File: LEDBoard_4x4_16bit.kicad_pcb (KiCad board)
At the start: 2 copper layers, 40 x 40 mm, 34 parts, among them J1 VCC_in, J2 GND_in, J3 signal_in, J4 VCC_out, J5 GND_out, J6 signal_out, U1 TLC5971RGER, U2 TLC5971RGER, U3 TLC5971RGER, U4 TLC5971RGER

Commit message: pcb parts all positioned
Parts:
- removed the J1 at (52.0, 60.0)
- removed J4: VCC_out, Socket_Strips:Socket_Strip_Angled_1x01_Pitch2.54mm
- removed J5: GND_out, Socket_Strips:Socket_Strip_Angled_1x01_Pitch2.54mm
- added C5: 47uF, Capacitors_SMD:C_0603, F.Cu at (70.0, 67.5)
- added HS1: Heatsink, Oddities:Dummy_Empty, F.Cu at (92.0, 90.0)
- added MK1: Mounting_Hole, Mounting_Holes:MountingHole_2.7mm_M2.5_Pad_Via, F.Cu at (60.0, 68.0)
- added MK2: Mounting_Hole, Mounting_Holes:MountingHole_2.7mm_M2.5_Pad_Via, F.Cu at (80.0, 68.0)
- J1: renamed from J3; moved to B.Cu
- J2: value GND_in -> power; footprint Socket_Strips:Socket_Strip_Angled_1x01_Pitch2.54mm -> Socket_Strips:Socket_Strip_Straight_1x06_Pitch2.54mm; moved to B.Cu
- J6: footprint Socket_Strips:Socket_Strip_Angled_1x02_Pitch2.54mm -> Socket_Strips:Socket_Strip_Straight_1x02_Pitch2.54mm; moved to B.Cu
- R1: value R -> 2k7 1%
- U1, U2, U3, U4: footprint Housings_DFN_QFN:QFN-24-1EP_4x4mm_Pitch0.5mm -> Housings_DFN_QFN:Texas_S-PVQFN-N24_ThermalVias
- moved J6 17.1 mm to (83.7, 88.0), turned to 270 degrees
- moved J1 16.8 mm to (53.7, 88.0), turned to 270 degrees
- moved J2 14.1 mm to (63.6, 88.0), turned to 270 degrees
- moved C4 10.2 mm to (85.0, 79.0), turned to 0 degrees
- moved R4 10.2 mm to (85.0, 77.0), turned to 0 degrees
- moved R1 4.12 mm to (65.0, 57.0)
- moved C3 2.24 mm to (65.0, 79.0)
- moved R2 2.24 mm to (85.0, 57.0)
- moved R3 2.24 mm to (65.0, 77.0)
- moved C2 2.14 mm to (85.0, 59.0)
- moved D1.1 2.00 mm to (55.0, 53.0)
- moved D1.2 2.00 mm to (55.0, 63.0)
- moved D1.3 2.00 mm to (55.0, 73.0)
- moved D1.4 2.00 mm to (55.0, 83.0)
- moved D2.1 2.00 mm to (65.0, 53.0)
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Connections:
- J2 pad 1: GND -> VCC
- U2 pad 6: /data_1-2 -> Net-(U2-Pad6)
- U3 pad 6: /data_2-3 -> Net-(U3-Pad6)
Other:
- board text added: "17.04.2017"
- board text added: "17.07. 2017"
- board text added: "LEDBoard 4x4 16bit"
- board text added: "LEDBoard_4x4_16bit cc by s-light.eu"
- board text added: "cc by s-light.eu"

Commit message: pcb started routing
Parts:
- D1.1, D1.2, D1.3, D1.4, D2.1, D2.2, D2.3, D2.4, D3.1, D3.2, D3.3, D3.4, D4.1, D4.2, D4.3, D4.4: footprint nichia:LED_NSSM032AT_wViaHeatSink -> nichia:LED_NSSM032AT_wViaHeatSinkBig
- MK1, MK2: footprint Mounting_Holes:MountingHole_2.7mm_M2.5_Pad_Via -> Mounting_Holes:MountingHole_3.2mm_M3_ISO7380_Pad
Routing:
- net VCC: track 0.00 -> 184.3 mm
- net GND: track 0.00 -> 88.3 mm
- net /LED_3.1_G: track 0.00 -> 35.7 mm, vias 0 -> 4
- net /LED_4.1_B: track 0.00 -> 35.0 mm
- net /LED_3.2_R: track 0.00 -> 33.8 mm, vias 0 -> 4
- net /LED_3.1_B: track 0.00 -> 33.6 mm, vias 0 -> 4
- net /LED_4.1_G: track 0.00 -> 32.1 mm
- net /LED_4.1_R: track 0.00 -> 31.0 mm
- net /LED_3.1_R: track 0.00 -> 30.8 mm, vias 0 -> 4
- net /LED_3.2_G: track 0.00 -> 30.1 mm, vias 0 -> 4
- net /LED_4.2_R: track 0.00 -> 28.1 mm
- net /LED_3.2_B: track 0.00 -> 26.6 mm, vias 0 -> 4
- net /LED_4.2_G: track 0.00 -> 22.4 mm
- net /LED_4.2_B: track 0.00 -> 16.8 mm
- net Net-(U2-Pad6): track 0.00 -> 10.7 mm, vias 0 -> 4
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
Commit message: pcb routing almost finished
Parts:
- moved C5 0.50 mm to (70.0, 68.0)
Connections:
- U4 pad 6: Net-(U4-Pad6) -> /data_out
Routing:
- net VCC: track 184.3 -> 325.1 mm
- net GND: track 88.3 -> 199.4 mm, vias 0 -> 6
- net /clock_in: track 0.00 -> 41.4 mm, vias 0 -> 1
- net /data_in: track 0.00 -> 40.4 mm, vias 0 -> 1
- net /data_1-2: track 0.00 -> 36.7 mm, vias 0 -> 3
- net /clock_1-2: track 10.7 -> 42.7 mm
- net /LED_3.1_G: track 35.7 -> 8.92 mm, vias 4 -> 1
- net /LED_4.1_B: track 35.0 -> 8.74 mm
- net /LED_3.2_R: track 33.8 -> 8.45 mm, vias 4 -> 1
- net /LED_3.1_B: track 33.6 -> 8.39 mm, vias 4 -> 1
- net /clock_2-3: track 0.00 -> 24.6 mm, vias 0 -> 4
- net /data_2-3: track 0.00 -> 24.5 mm, vias 0 -> 3
- net /LED_4.1_G: track 32.1 -> 8.02 mm
- net /LED_4.1_R: track 31.0 -> 7.76 mm
- net /LED_3.1_R: track 30.8 -> 7.69 mm, vias 4 -> 1
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- added copper zone on F.Cu, net GND
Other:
- net class signal added: clearance 0.15, trace_width 0.2, via_dia 0.6, via_drill 0.3

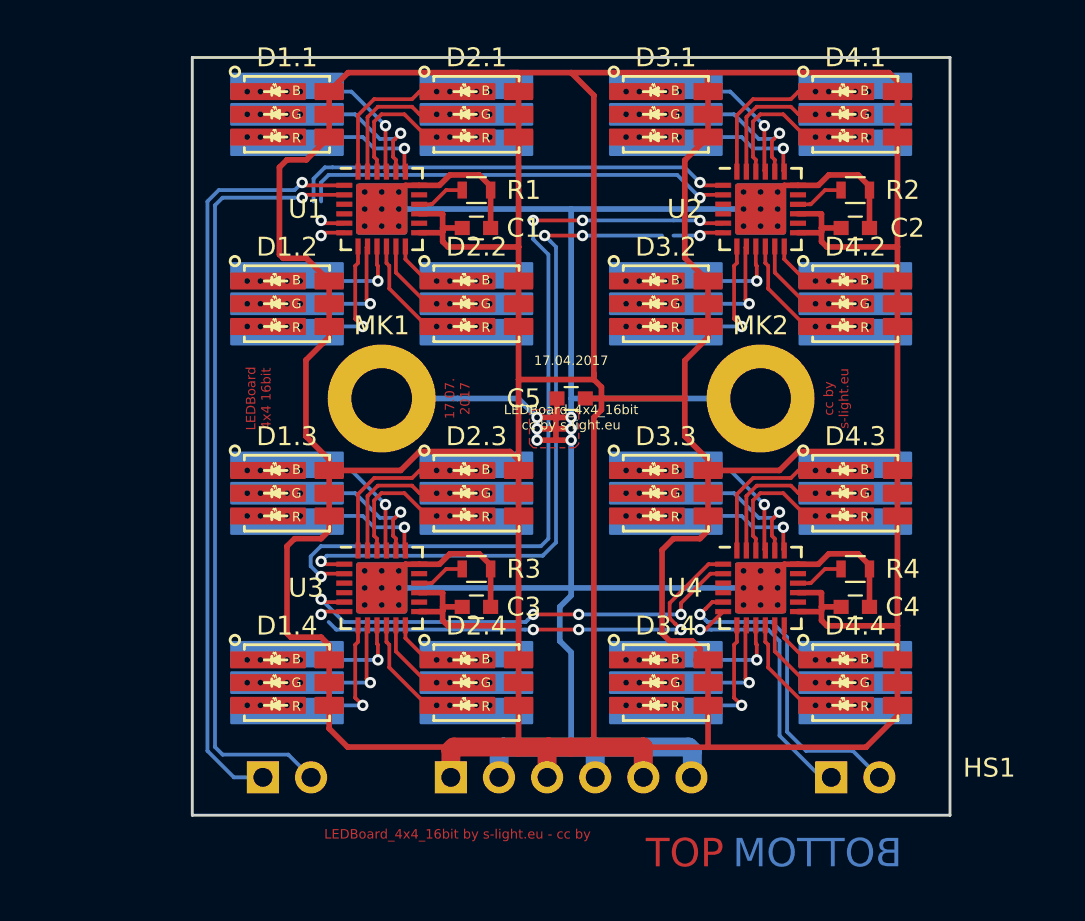
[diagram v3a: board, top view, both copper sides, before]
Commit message: pcb tried to fix missing net links
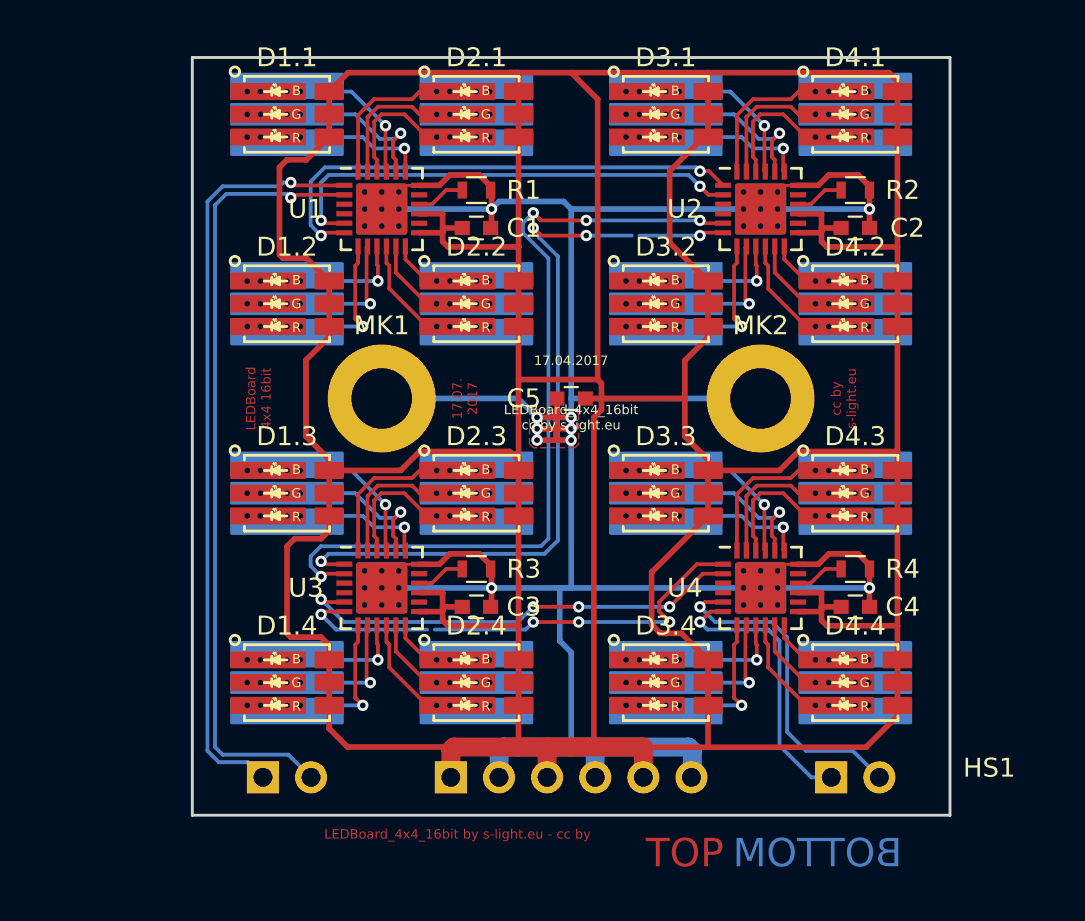
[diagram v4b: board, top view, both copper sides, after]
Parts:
- R2, R3, R4: value R -> 2k7 1%
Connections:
- net /data_1-2 renamed /data_intern_2
- net Net-(R1-Pad1) renamed /U1_sense
- net Net-(R2-Pad1) renamed /U2_sense
- net Net-(R3-Pad1) renamed /U3_sense
- net Net-(R4-Pad1) renamed /U4_sense
- U4 pad 1: /data_2-3 -> Net-(U3-Pad6)
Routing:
- net GND: track 199.4 -> 160.4 mm, vias 6 -> 10
- net /data_2-3: track 24.5 -> 0.00 mm, vias 3 -> 0
- net Net-(U3-Pad6): track 1.29 -> 25.3 mm, vias 1 -> 4
- net /LED_4.4_B: track 4.20 -> 7.30 mm
- net /LED_4.4_R: track 7.02 -> 10.1 mm
- net /LED_4.4_G: track 5.61 -> 8.41 mm
- net /data_0-1: track 24.8 -> 26.8 mm
- net Net-(U2-Pad6): track 2.69 -> 4.49 mm
- net /clock_1-2: track 42.7 -> 43.8 mm
- net /clock_0-1: track 24.2 -> 25.2 mm
- net /clock_2-3: track 24.6 -> 24.1 mm
- added copper zone on B.Cu, net GND
- added copper zone on F.Cu, net VCC

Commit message: pcb fixed broken net data_2-3
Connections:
- net /data_intern_2 renamed /data_1-2
- net Net-(U3-Pad6) renamed /data_2-3

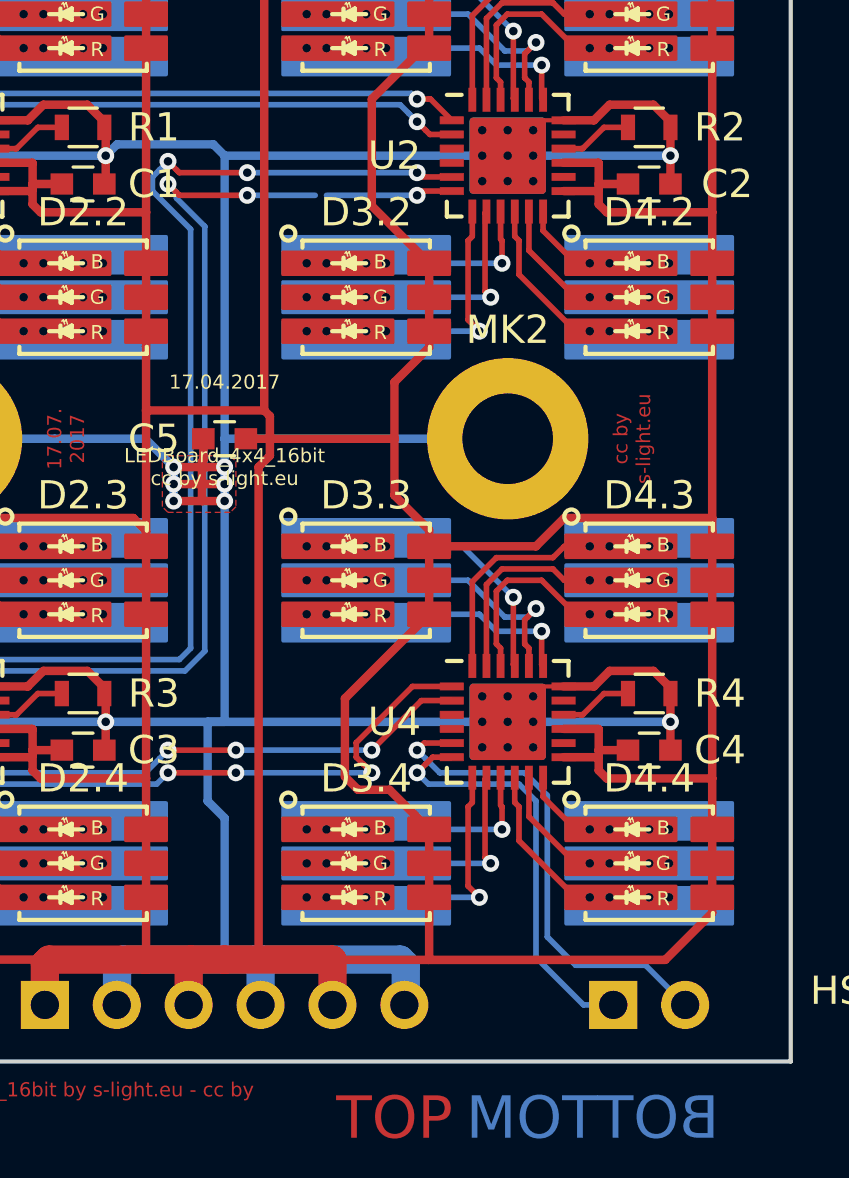
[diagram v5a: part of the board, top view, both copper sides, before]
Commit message: fixed net data_1-2 (manually hand edited net-file)
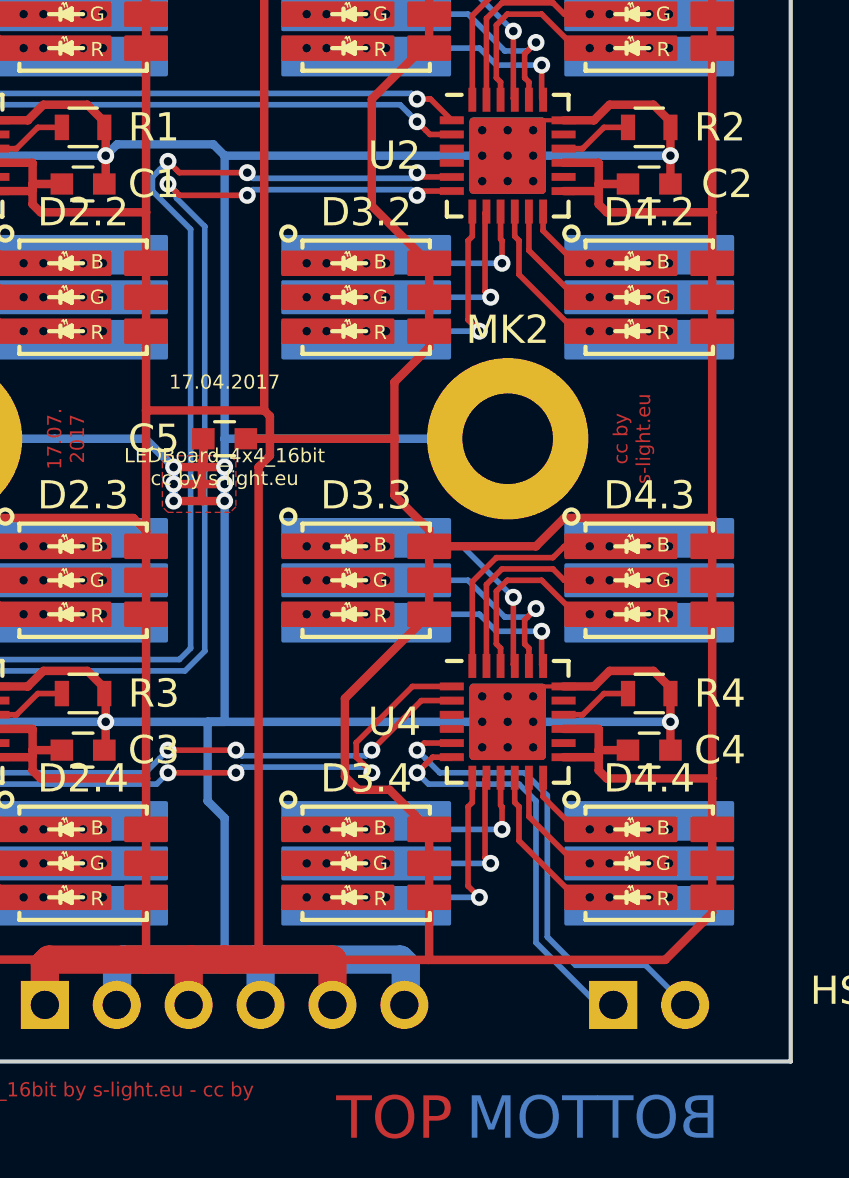
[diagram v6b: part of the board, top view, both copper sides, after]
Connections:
- U2 pad 6: Net-(U2-Pad6) -> /data_1-2
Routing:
- net /data_1-2: track 36.6 -> 41.7 mm, vias 3 -> 4
- net Net-(U2-Pad6): track 4.49 -> 0.00 mm, vias 1 -> 0
